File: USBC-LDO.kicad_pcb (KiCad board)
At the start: 2 copper layers, 25 x 13 mm, 9 parts, among them J1 USB_C_Receptacle_USB2.0_16P, J2 Conn_01x05_Pin, U1 AMS1117-3.3

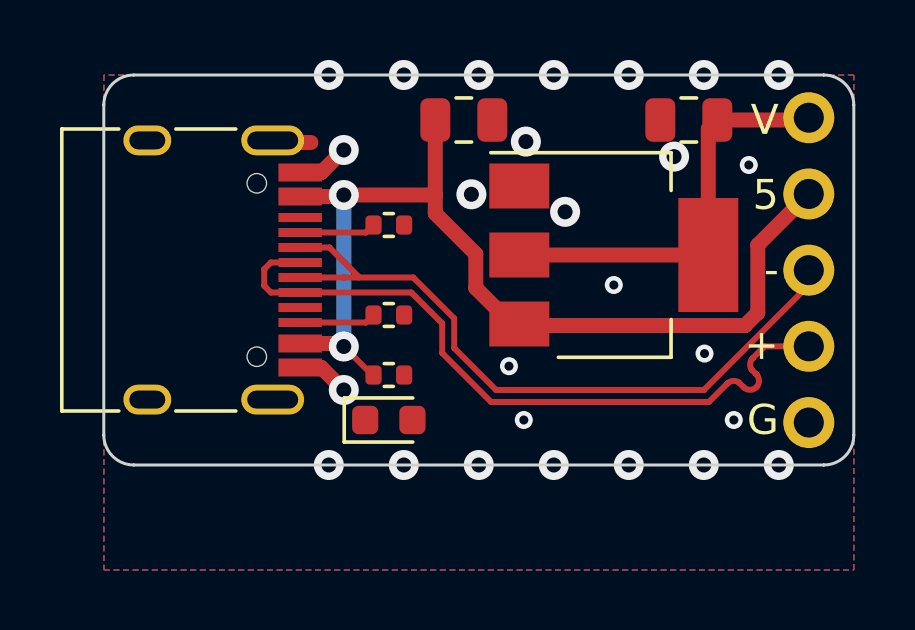
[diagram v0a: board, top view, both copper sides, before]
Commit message: Added proper 3D model for USB-C port.
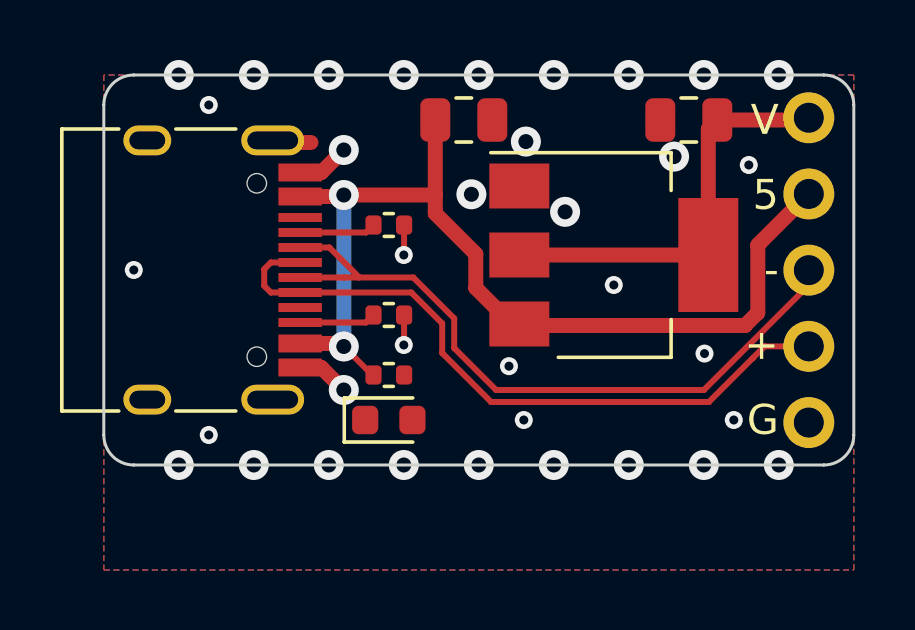
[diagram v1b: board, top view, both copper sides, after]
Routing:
- net GND: track 3.53 -> 5.54 mm, vias 26 -> 35
- net /D+: track 24.0 -> 23.0 mm
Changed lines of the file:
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@@
     (property "ki_keywords" "usb universal serial bus type-C USB2.0")
     (attr smd)
-    (fp_text reference "J1" (at 0 -5.645 -90) (layer "F.SilkS") hide
-        (effects (font (size 1 1) (thickness 0.15)))
-    )
-    (fp_text value "USB_C_Receptacle_USB2.0_16P" (at 0 5.1 -90) (layer "F.Fab")
-        (effects (font (size 1 1) (thickness 0.15)))
-    )
-    (fp_text user "${REFERENCE}" (at 0 0 -90) (layer "F.Fab")
+    (fp_text reference "J1" (at 0 -5.645 90) (layer "F.SilkS") hide
+        (effects (font (size 1 1) (thickness 0.15)))
+    )
+    (fp_text value "USB_C_Receptacle_USB2.0_16P" (at 0 5.1 90) (layer "F.Fab")
+        (effects (font (size 1 1) (thickness 0.15)))
+    )
+    (fp_text user "${REFERENCE}" (at 0 0 90) (layer "F.Fab")
         (effects (font (size 1 1) (thickness 0.15)))
     )
@@
     (pad "S1" thru_hole oval (at 4.32 1.05 270) (size 1 1.6) (drill oval 0.6 1.2) (layers "*.Cu" "*.Mask")
       (net 11 "unconnected-(J1-SHIELD-PadS1)") (pinfunction "SHIELD") (pintype "passive+no_connect"))
-    (model "${KICAD6_3DMODEL_DIR}/Connector_USB.3dshapes/USB_C_Receptacle_HRO_TYPE-C-31-M-12.wrl"
+    (model "${KICAD7_3DMODEL_DIR}/Connector_USB.3dshapes/USB_C_Receptacle_GCT_USB4105-xx-A_16P_TopMnt_Horizontal.wrl"
       (offset (xyz 0 0 0))
       (scale (xyz 1 1 1))
@@
   (gr_arc (start 170 105.5) (mid 169.707107 106.207107) (end 169 106.5)
     (stroke (width 0.1) (type default)) (layer "Edge.Cuts"))
-  (gr_text "${TITLE}" (at 158 98.5) (layer "B.SilkS")
+  (gr_text "${TITLE}" (at 156 98.5) (layer "B.SilkS")
     (effects (font (size 1 1) (thickness 0.15)) (justify mirror))
   )
@@
     (effects (font (size 1 1) (thickness 0.15)) (justify left mirror))
   )
-  (gr_text "${COMPANY}" (at 158 101.5) (layer "B.SilkS")
+  (gr_text "${COMPANY}" (at 156 101.5) (layer "B.SilkS")
     (effects (font (size 1 1) (thickness 0.15)) (justify mirror))
   )
@@
   (via (at 153 97.5) (size 1) (drill 0.5) (layers "F.Cu" "B.Cu") (net 1))
   (segment (start 153 97.5) (end 153 102.55) (width 0.5) (layer "B.Cu") (net 1))
+  (segment (start 155.01 102.49) (end 155 102.5) (width 0.2) (layer "F.Cu") (net 2))
   (segment (start 152.25 103.25) (end 153 104) (width 0.5) (layer "F.Cu") (net 2))
+  (segment (start 155.01 98.5) (end 155.01 99.49) (width 0.2) (layer "F.Cu") (net 2))
+  (segment (start 155.01 99.49) (end 155 99.5) (width 0.2) (layer "F.Cu") (net 2))
   (segment (start 151.545 96.75) (end 152.25 96.75) (width 0.5) (layer "F.Cu") (net 2))
+  (segment (start 155.01 101.5) (end 155.01 102.49) (width 0.2) (layer "F.Cu") (net 2))
   (segment (start 151.545 103.25) (end 152.25 103.25) (width 0.5) (layer "F.Cu") (net 2))
   (segment (start 152.25 96.75) (end 153 96) (width 0.5) (layer "F.Cu") (net 2))
+  (via (at 148.5 94.5) (size 0.6) (drill 0.3) (layers "F.Cu" "B.Cu") (free) (net 2))
   (via (at 160 106.5) (size 1) (drill 0.5) (layers "F.Cu" "B.Cu") (free) (net 2))
+  (via (at 150 106.5) (size 1) (drill 0.5) (layers "F.Cu" "B.Cu") (free) (net 2))
   (via (at 155 93.5) (size 1) (drill 0.5) (layers "F.Cu" "B.Cu") (free) (net 2))
+  (via (at 146 100) (size 0.6) (drill 0.3) (layers "F.Cu" "B.Cu") (free) (net 2))
   (via (at 159 105) (size 0.6) (drill 0.3) (layers "F.Cu" "B.Cu") (free) (net 2))
   (via (at 166.5 96.5) (size 0.6) (drill 0.3) (layers "F.Cu" "B.Cu") (free) (net 2))
   (via (at 165 93.5) (size 1) (drill 0.5) (layers "F.Cu" "B.Cu") (free) (net 2))
+  (via (at 155 102.5) (size 0.6) (drill 0.3) (layers "F.Cu" "B.Cu") (net 2))
   (via (at 152.5 93.5) (size 1) (drill 0.5) (layers "F.Cu" "B.Cu") (free) (net 2))
   (via (at 162.5 106.5) (size 1) (drill 0.5) (layers "F.Cu" "B.Cu") (free) (net 2))
@@
   (via (at 160.376419 98.061646) (size 1) (drill 0.5) (layers "F.Cu" "B.Cu") (free) (net 2))
   (via (at 153 96) (size 1) (drill 0.5) (layers "F.Cu" "B.Cu") (net 2))
+  (via (at 147.5 106.5) (size 1) (drill 0.5) (layers "F.Cu" "B.Cu") (free) (net 2))
   (via (at 165.023912 102.785812) (size 0.6) (drill 0.3) (layers "F.Cu" "B.Cu") (free) (net 2))
   (via (at 157.253125 97.476029) (size 1) (drill 0.5) (layers "F.Cu" "B.Cu") (free) (net 2))
@@
   (via (at 159.069388 95.719176) (size 1) (drill 0.5) (layers "F.Cu" "B.Cu") (free) (net 2))
   (via (at 158.505734 103.205929) (size 0.6) (drill 0.3) (layers "F.Cu" "B.Cu") (free) (net 2))
+  (via (at 150 93.5) (size 1) (drill 0.5) (layers "F.Cu" "B.Cu") (free) (net 2))
   (via (at 152.5 106.5) (size 1) (drill 0.5) (layers "F.Cu" "B.Cu") (free) (net 2))
+  (via (at 148.5 105.5) (size 0.6) (drill 0.3) (layers "F.Cu" "B.Cu") (free) (net 2))
   (via (at 162.5 93.5) (size 1) (drill 0.5) (layers "F.Cu" "B.Cu") (free) (net 2))
   (via (at 160 93.5) (size 1) (drill 0.5) (layers "F.Cu" "B.Cu") (free) (net 2))
+  (via (at 147.5 93.5) (size 1) (drill 0.5) (layers "F.Cu" "B.Cu") (free) (net 2))
   (via (at 162 100.5) (size 0.6) (drill 0.3) (layers "F.Cu" "B.Cu") (free) (net 2))
+  (via (at 155 99.5) (size 0.6) (drill 0.3) (layers "F.Cu" "B.Cu") (net 2))
   (via (at 157.5 106.5) (size 1) (drill 0.5) (layers "F.Cu" "B.Cu") (free) (net 2))
   (via (at 164.009232 96.219922) (size 1) (drill 0.5) (layers "F.Cu" "B.Cu") (free) (net 2))
@@
   (segment (start 153 100.25) (end 151.545 100.25) (width 0.2) (layer "F.Cu") (net 5))
   (segment (start 153.5 100.23) (end 153.5 100.25) (width 0.2) (layer "F.Cu") (net 5))
-  (segment (start 165.168186 104.4) (end 165.784093 103.784093) (width 0.2) (layer "F.Cu") (net 6))
-  (segment (start 151.545 100.75) (end 155.25 100.75) (width 0.2) (layer "F.Cu") (net 6))
+  (segment (start 165.168186 104.4) (end 166.63262 102.935566) (width 0.2) (layer "F.Cu") (net 6))
+  (segment (start 156.280593 101.780593) (end 156.280593 102.767985) (width 0.2) (layer "F.Cu") (net 6))
+  (segment (start 157.912608 104.4) (end 165.168186 104.4) (width 0.2) (layer "F.Cu") (net 6))
   (segment (start 151.545 99.75) (end 150.57 99.75) (width 0.2) (layer "F.Cu") (net 6))
   (segment (start 150.57 100.75) (end 151.545 100.75) (width 0.2) (layer "F.Cu") (net 6))
   (segment (start 150.346078 100.526078) (end 150.57 100.75) (width 0.2) (layer "F.Cu") (net 6))
-  (segment (start 166.632621 102.935564) (end 167.023186 102.545) (width 0.2) (layer "F.Cu") (net 6))
-  (segment (start 166.174025 103.751504) (end 166.328174 103.905653) (width 0.2) (layer "F.Cu") (net 6))
+  (segment (start 156.280593 102.767985) (end 157.912608 104.4) (width 0.2) (layer "F.Cu") (net 6))
+  (segment (start 151.545 100.75) (end 155.25 100.75) (width 0.2) (layer "F.Cu") (net 6))
   (segment (start 150.57 99.75) (end 150.346078 99.973922) (width 0.2) (layer "F.Cu") (net 6))
+  (segment (start 167.023186 102.545) (end 168.5 102.545) (width 0.2) (layer "F.Cu") (net 6))
   (segment (start 155.25 100.75) (end 156.280593 101.780593) (width 0.2) (layer "F.Cu") (net 6))
-  (segment (start 156.280593 101.780593) (end 156.280593 102.767985) (width 0.2) (layer "F.Cu") (net 6))
-  (segment (start 166.328174 103.905653) (end 166.328174 103.905755) (width 0.2) (layer "F.Cu") (net 6))
-  (segment (start 166.752438 103.477896) (end 166.600036 103.325494) (width 0.2) (layer "F.Cu") (net 6))
-  (segment (start 166.63262 102.935563) (end 166.632621 102.935564) (width 0.2) (layer "F.Cu") (net 6))
-  (segment (start 166.752438 103.481489) (end 166.752438 103.477896) (width 0.2) (layer "F.Cu") (net 6))
-  (segment (start 167.023186 102.545) (end 168.5 102.545) (width 0.2) (layer "F.Cu") (net 6))
-  (segment (start 157.912608 104.4) (end 165.168186 104.4) (width 0.2) (layer "F.Cu") (net 6))
   (segment (start 151.545 100.75) (end 151.595 100.7) (width 0.2) (layer "F.Cu") (net 6))
+  (segment (start 166.63262 102.935566) (end 167.023186 102.545) (width 0.2) (layer "F.Cu") (net 6))
   (segment (start 150.346078 99.973922) (end 150.346078 100.526078) (width 0.2) (layer "F.Cu") (net 6))
-  (segment (start 166.752438 103.481489) (end 166.752438 103.48149) (width 0.2) (layer "F.Cu") (net 6))
-  (segment (start 156.280593 102.767985) (end 157.912608 104.4) (width 0.2) (layer "F.Cu") (net 6))
-  (arc (start 166.600036 103.325494) (mid 166.545687 103.12416) (end 166.63262 102.935563) (width 0.2) (layer "F.Cu") (net 6))
-  (arc (start 165.784093 103.784093) (mid 165.972687 103.69715) (end 166.174025 103.751504) (width 0.2) (layer "F.Cu") (net 6))
-  (arc (start 166.328174 103.905755) (mid 166.540306 103.993623) (end 166.752438 103.905755) (width 0.2) (layer "F.Cu") (net 6))
-  (arc (start 166.752438 103.905755) (mid 166.840306 103.693622) (end 166.752438 103.481489) (width 0.2) (layer "F.Cu") (net 6))
   (segment (start 153.74 98.75) (end 153.99 98.5) (width 0.2) (layer "F.Cu") (net 7))
   (segment (start 151.545 98.75) (end 153.74 98.75) (width 0.2) (layer "F.Cu") (net 7))

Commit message: Fixed missing trace
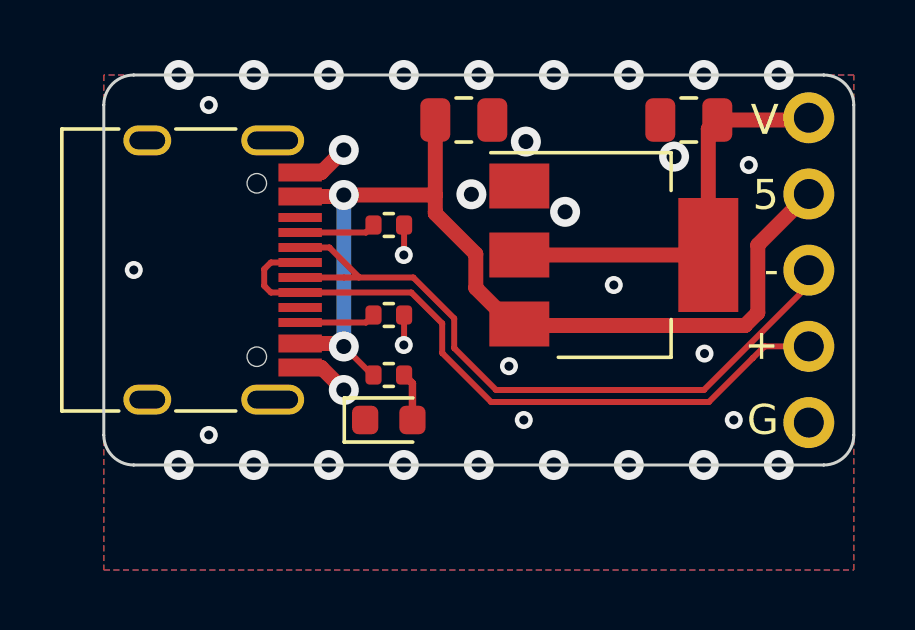
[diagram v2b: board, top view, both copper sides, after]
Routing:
- net Net-(D1-A): track 0.00 -> 1.61 mm
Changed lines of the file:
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@@
   (segment (start 165.45 95) (end 168.425 95) (width 0.5) (layer "F.Cu") (net 3))
   (segment (start 165.15 99.5) (end 165.15 95.3) (width 0.5) (layer "F.Cu") (net 3))
+  (segment (start 155.2875 103.7775) (end 155.01 103.5) (width 0.25) (layer "F.Cu") (net 4))
+  (segment (start 155.2875 105) (end 155.2875 103.7775) (width 0.25) (layer "F.Cu") (net 4))
   (segment (start 156.680593 102.6023) (end 156.680593 101.614908) (width 0.2) (layer "F.Cu") (net 5))
   (segment (start 152.52 99.25) (end 153.5 100.23) (width 0.2) (layer "F.Cu") (net 5))
@@
   (segment (start 153.74 101.75) (end 153.99 101.5) (width 0.2) (layer "F.Cu") (net 9))
   (segment (start 151.545 101.75) (end 153.74 101.75) (width 0.2) (layer "F.Cu") (net 9))
-  (segment (start 151.545 95.75) (end 151.906496 95.75) (width 0.5) (layer "F.Cu") (net 11))
   (zone (net 2) (net_name "GND") (layers "F&B.Cu") (hatch edge 0.5)
     (connect_pads yes (clearance 0.25))
